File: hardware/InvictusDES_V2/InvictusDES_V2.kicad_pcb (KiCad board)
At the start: 4 copper layers, 53.7 x 40.9 mm, 73 parts, among them J1 Screw_Terminal_01x02, J10 USB_B_Micro, J11 Conn_01x06, J12 Micro_SD_Card, J2 Conn_02x05_Odd_Even, J3 Conn_01x06, J9 Conn_01x04, U1 TPSM863257RDXR, U2 STM32F405RGTx, U3 TPS2116DRL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

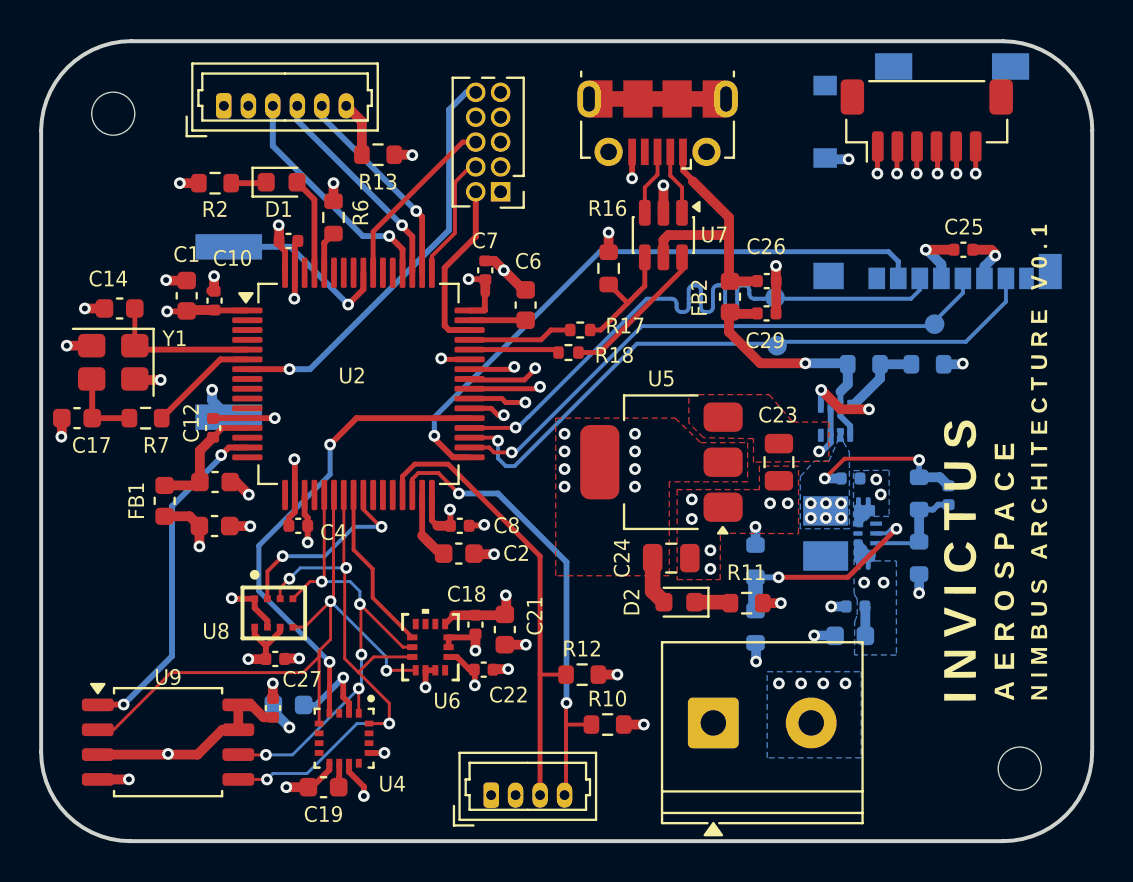
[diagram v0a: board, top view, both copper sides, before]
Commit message: Connectors made to JST-SH, aligned silkscreen designators and connectors
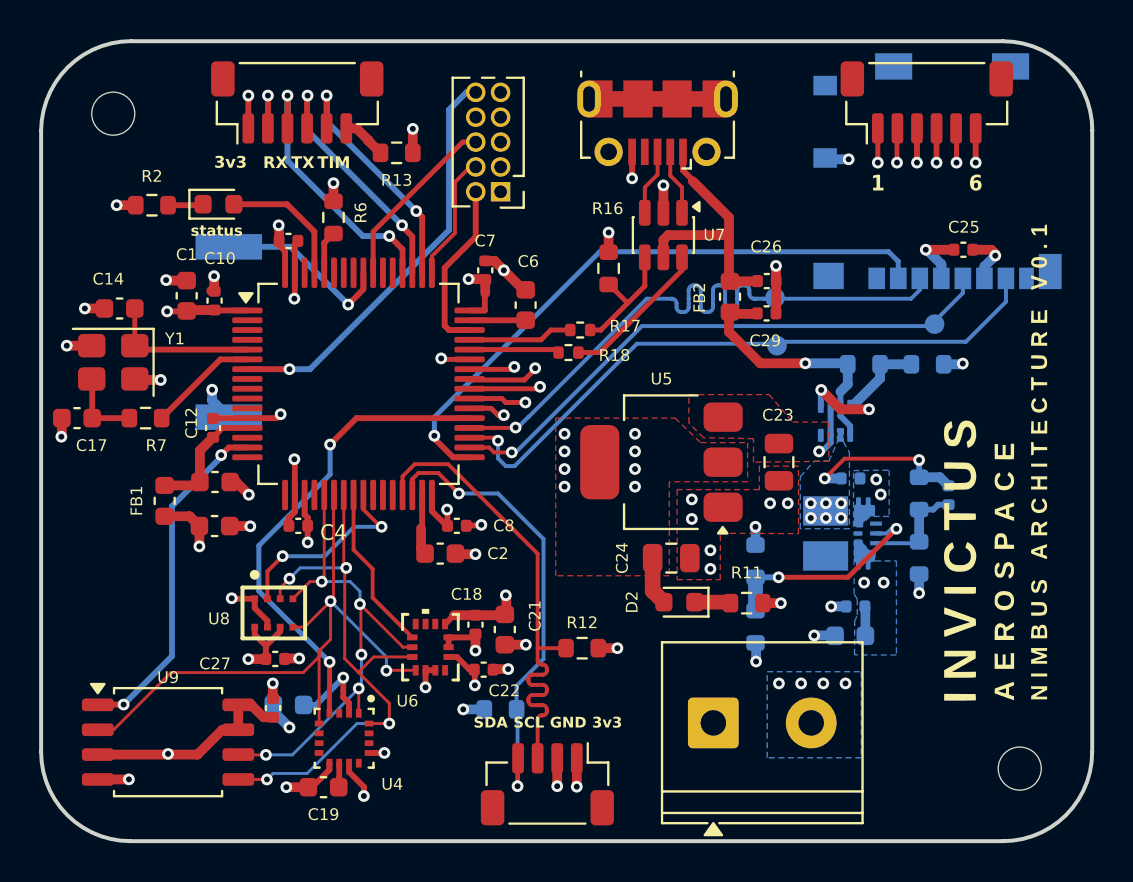
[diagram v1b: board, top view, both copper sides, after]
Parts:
- J11: footprint Connector_Molex:Molex_PicoBlade_53047-0610_1x06_P1.25mm_Vertical -> Connector_JST:JST_SH_BM06B-SRSS-TB_1x06-1MP_P1.00mm_Vertical
- J9: footprint Connector_Molex:Molex_PicoBlade_53047-0410_1x04_P1.25mm_Vertical -> Connector_JST:JST_SH_BM04B-SRSS-TB_1x04-1MP_P1.00mm_Vertical
- R10: moved to B.Cu
- moved R10 5.53 mm to (118.6, 121.1), turned to 0 degrees
- moved J11 3.75 mm to (108.2, 90.1)
- moved D1 3.42 mm to (104.2, 95.3)
- moved R2 3.42 mm to (100.8, 95.4)
- moved J9 2.93 mm to (121.0, 125.0), turned to 180 degrees
- moved R12 1.35 mm to (122.8, 118.0)
- moved R13 0.95 mm to (113.3, 92.7)
- moved C2 0.95 mm to (115.5, 113.2)
- moved J3 0.92 mm to (140.3, 90.1)
- moved C8 0.15 mm to (116.3, 111.8)
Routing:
- net GND: track 70.2 -> 73.7 mm, vias 49 -> 51
- net +3V3: track 55.7 -> 58.7 mm, vias 25 -> 27
- net USART3_TX: track 11.0 -> 13.6 mm, vias 1 -> 2
- net TIM2_CH1: track 10.6 -> 12.8 mm, vias 1 -> 2
- net USART3_RX: track 12.1 -> 13.9 mm, vias 1 -> 2
- net LED_STATUS: track 4.99 -> 6.79 mm
- net I2C2_SCL: track 23.7 -> 25.4 mm
- net SERVO_4: track 31.1 -> 32.1 mm
- net SERVO_3: track 29.9 -> 30.9 mm
- net SERVO_1: track 30.2 -> 31.1 mm
- net SERVO_2: track 28.8 -> 29.7 mm
- net SERVO_5: track 33.2 -> 34.1 mm
- net SERVO_6: track 35.2 -> 36.0 mm
- net Net-(J11-Pin_6): track 2.83 -> 2.28 mm
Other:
- board text added: "1"
- board text added: "3v3"
- board text added: "6"
- board text added: "GND"
- board text added: "RX"
- board text added: "SCL"
- board text added: "SDA"
- board text added: "TIM"
- board text added: "TX"
- board text added: "status"

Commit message: keep-out zones for IMU, Mag filled.
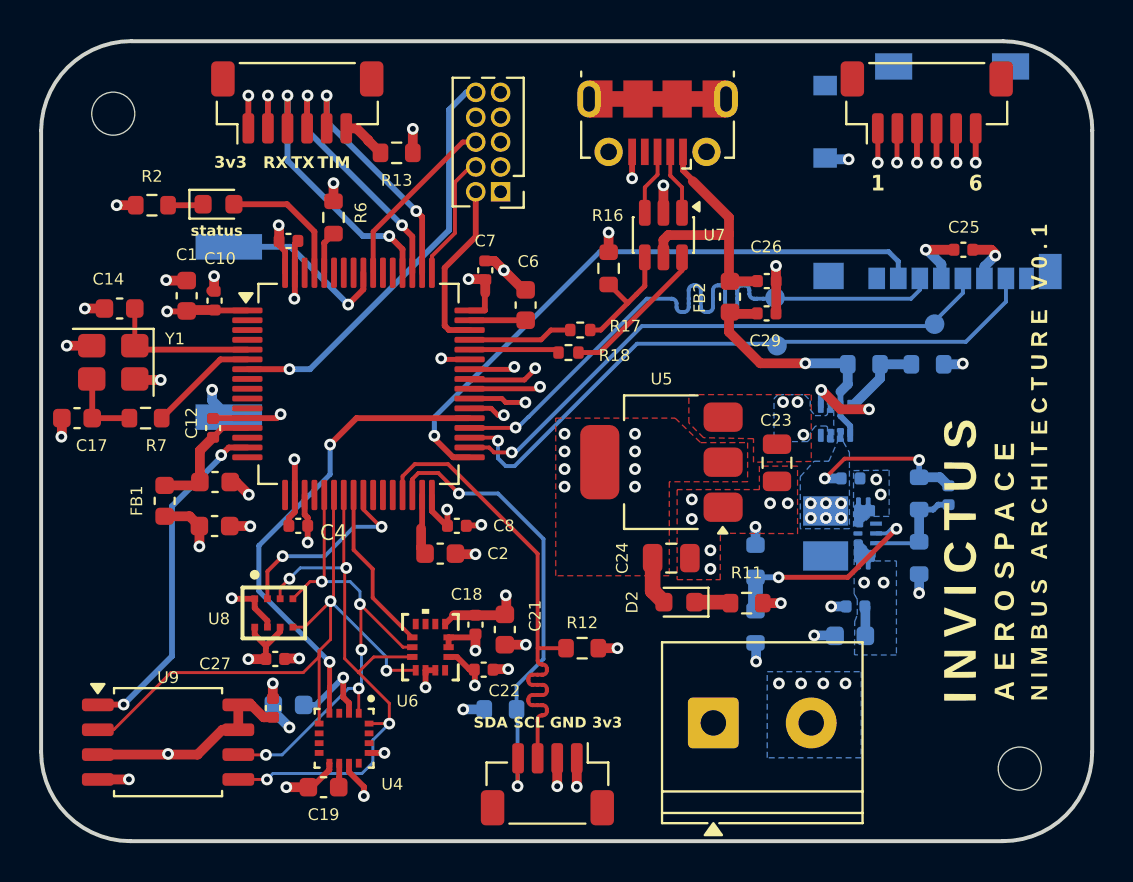
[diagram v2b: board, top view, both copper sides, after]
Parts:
- moved C23 0.10 mm to (132.7, 108.5)
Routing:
- net 5V_MUX: track 2.74 -> 0.11 mm, vias 1 -> 3
- net SPI1_MOSI: track 30.1 -> 30.7 mm
- added copper zone on B.Cu, net 5V_MUX
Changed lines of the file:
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@@
 			(outputformat 1)
 			(mirror no)
-			(drillshape 1)
+			(drillshape 0)
 			(scaleselection 1)
-			(outputdirectory "")
+			(outputdirectory "./")
 		)
 	)
@@
 		(tags "resistor")
 		(property "Reference" "R16"
-			(at 3.05 -0.05 0)
+			(at 2.7 -0.05 0)
 			(layer "F.SilkS")
 			(effects
@@
 	(footprint "Capacitor_SMD:C_0805_2012Metric"
 		(layer "F.Cu")
-		(at 132.8 108.5 -90)
+		(at 132.7 108.53 -90)
 		(descr "Capacitor SMD 0805 (2012 Metric), square (rectangular) end terminal, IPC-7351 nominal, (Body size source: IPC-SM-782 page 76, https://www.pcb-3d.com/wordpress/wp-content/uploads/ipc-sm-782a_amendment_1_and_2.pdf, https://docs.google.com/spreadsheets/d/1BsfQQcO9C6DZCsRaXUlFlo91Tg2WpOkGARC1WS5S8t0/edit?usp=sharing), generated with kicad-footprint-generator")
 		(tags "capacitor")
@@
 		)
 		(fp_text user "${REFERENCE}"
-			(at -2.4 0.05 180)
+			(at -2.17 0.05 180)
 			(layer "F.SilkS")
 			(effects
@@
 		(tags "SOT-583-8")
 		(property "Reference" "U3"
-			(at 0.161875 2.39 0)
+			(at -1.958125 1.78 0)
 			(unlocked yes)
 			(layer "B.SilkS")
@@
 	)
 	(via
-		(at 134.85 107.95)
+		(at 133.01 105.43)
 		(size 0.6)
 		(drill 0.3)
 		(layers "F.Cu" "B.Cu")
+		(free yes)
 		(net 7)
 	)
-	(segment
-		(start 135.44 107.513729)
-		(end 135.003729 107.95)
-		(width 0.3)
-		(layer "B.Cu")
-		(net 7)
-	)
-	(segment
-		(start 135.44 107.128125)
-		(end 135.44 105.648125)
-		(width 0.3)
-		(layer "B.Cu")
-		(net 7)
-	)
-	(segment
-		(start 135.003729 107.95)
-		(end 134.85 107.95)
-		(width 0.3)
-		(layer "B.Cu")
+	(via
+		(at 134.05 107.1)
+		(size 0.6)
+		(drill 0.3)
+		(layers "F.Cu" "B.Cu")
+		(free yes)
 		(net 7)
 	)
-	(segment
-		(start 135.44 107.128125)
-		(end 135.44 107.513729)
-		(width 0.3)
-		(layer "B.Cu")
+	(via
+		(at 133.75 105.43)
+		(size 0.6)
+		(drill 0.3)
+		(layers "F.Cu" "B.Cu")
+		(free yes)
 		(net 7)
 	)
@@
 	)
 	(segment
-		(start 135.94 105.648125)
-		(end 135.94 104.898125)
+		(start 135.94 106.146875)
+		(end 135.94 105.648125)
 		(width 0.3)
 		(layer "B.Cu")
@@
 	)
 	(segment
-		(start 135.94 106.146875)
-		(end 135.94 105.648125)
-		(width 0.3)
+		(start 135.94 104.898125)
+		(end 136.315 104.523125)
+		(width 0.5)
 		(layer "B.Cu")
 		(net 17)
@@
 	)
 	(segment
-		(start 135.94 104.898125)
-		(end 136.315 104.523125)
-		(width 0.5)
+		(start 135.94 105.648125)
+		(end 135.94 104.898125)
+		(width 0.3)
 		(layer "B.Cu")
 		(net 17)
@@
 	)
 	(segment
+		(start 141.9 96.95)
+		(end 141.9 93.23)
+		(width 0.254)
+		(layer "In1.Cu")
+		(net 31)
+	)
+	(segment
 		(start 141.87 93.1)
 		(end 141.87 93.2)
@@
 	)
 	(segment
-		(start 133.4 105.45)
-		(end 119.85 105.45)
+		(start 141.9 93.23)
+		(end 141.87 93.2)
 		(width 0.254)
 		(layer "In1.Cu")
@@
 	)
 	(segment
-		(start 141.9 96.95)
-		(end 133.4 105.45)
+		(start 134.29 104.56)
+		(end 141.9 96.95)
 		(width 0.254)
 		(layer "In1.Cu")
@@
 	)
 	(segment
-		(start 141.87 93.2)
-		(end 141.9 93.23)
+		(start 119.85 105.45)
+		(end 131.53 105.45)
 		(width 0.254)
 		(layer "In1.Cu")
@@
 	)
 	(segment
-		(start 141.9 93.23)
-		(end 141.9 96.95)
+		(start 132.42 104.56)
+		(end 134.29 104.56)
+		(width 0.254)
+		(layer "In1.Cu")
+		(net 31)
+	)
+	(segment
+		(start 131.53 105.45)
+		(end 132.42 104.56)
 		(width 0.254)
 		(layer "In1.Cu")
@@
 	)
 	(segment
-		(start 112.9 121.85)
-		(end 111.25 121.85)
+		(start 106.65 124.705)
+		(end 106.955 124.4)
 		(width 0.15)
 		(layer "B.Cu")
@@
 	)
 	(segment
+		(start 112.06 122.69)
+		(end 112.9 121.85)
+		(width 0.15)
+		(layer "B.Cu")
+		(net 46)
+	)
+	(segment
 		(start 106.955 124.4)
-		(end 106.65 124.705)
+		(end 111.5 124.4)
 		(width 0.15)
 		(layer "B.Cu")
@@
 	)
 	(segment
-		(start 108.7 124.4)
-		(end 106.955 124.4)
+		(start 112.06 123.84)
+		(end 112.06 122.69)
 		(width 0.15)
 		(layer "B.Cu")
@@
 	)
 	(segment
-		(start 111.25 121.85)
-		(end 108.7 124.4)
+		(start 111.5 124.4)
+		(end 112.06 123.84)
 		(width 0.15)
 		(layer "B.Cu")
@@
 	)
 	(via
-		(at 111.477354 118.327354)
+		(at 111.477354 118.077354)
 		(size 0.6)
 		(drill 0.3)
@@
 	)
 	(segment
-		(start 111.338638 120.054577)
-		(end 111.345423 120.054577)
-		(width 0.15)
-		(layer "B.Cu")
-		(net 50)
-	)
-	(segment
 		(start 111.4 115.75)
 		(end 111.4 115.1)
@@
 	)
 	(segment
-		(start 111.345423 120.054577)
-		(end 111.477354 119.922646)
+		(start 107.42 123.45)
+		(end 106.6 123.45)
 		(width 0.15)
 		(layer "B.Cu")
@@
 	)
 	(segment
-		(start 111.338638 120.061362)
-		(end 107.95 123.45)
+		(start 111.4 115.1)
+		(end 110.9 114.6)
 		(width 0.15)
 		(layer "B.Cu")
@@
 	)
 	(segment
-		(start 111.4 115.1)
-		(end 110.9 114.6)
+		(start 111.338638 120.054577)
+		(end 110.815423 120.054577)
 		(width 0.15)
 		(layer "B.Cu")
@@
 	(segment
 		(start 111.477354 119.922646)
-		(end 111.477354 118.327354)
+		(end 111.345423 120.054577)
 		(width 0.15)
 		(layer "B.Cu")
@@
 	)
 	(segment
-		(start 107.95 123.45)
-		(end 106.6 123.45)
+		(start 110.815423 120.054577)
+		(end 107.42 123.45)
 		(width 0.15)
 		(layer "B.Cu")
@@
 	)
 	(segment
-		(start 111.338638 120.054577)
-		(end 111.338638 120.061362)
+		(start 111.345423 120.054577)
+		(end 111.338638 120.054577)
+		(width 0.15)
+		(layer "B.Cu")
+		(net 50)
+	)
+	(segment
+		(start 111.477354 118.077354)
+		(end 111.477354 119.922646)
 		(width 0.15)
 		(layer "B.Cu")
@@
 		(priority 4)
 		(connect_pads yes
-			(clearance 0.4)
+			(clearance 0.3)
 		)
 		(min_thickness 0.25)
@@
 		(polygon
 			(pts
-				(xy 133.8 108.7) (xy 131.8 108.7) (xy 131.8 109.9) (xy 127.6 109.9) (xy 127.6 114.5) (xy 129.8 114.5)
-				(xy 129.81 112.13) (xy 133.8 112.15)
+				(xy 133.75 108.7) (xy 131.8 108.7) (xy 131.8 109.9) (xy 127.6 109.9) (xy 127.6 114.5) (xy 129.8 114.5)
+				(xy 129.81 112.13) (xy 133.75 112.149747)
 			)
 		)
@@
 		(polygon
 			(pts
-				(xy 135.35 108.45) (xy 131.5 108.5) (xy 131.5 107.3) (xy 128.95 107.25) (xy 128.2 106.5) (xy 128.2 105.05)
-				(xy 132.3 105.05) (xy 133.5 106.45) (xy 135.35 106.45)
+				(xy 134.45 108.461688) (xy 131.5 108.5) (xy 131.5 107.3) (xy 128.95 107.25) (xy 128.2 106.5) (xy 128.2 105.05)
+				(xy 134.45 105.05)
 			)
 		)
@@
 	)
 	(zone
+		(net 0)
+		(net_name "")
+		(layers "F.Cu" "B.Cu" "In1.Cu" "In2.Cu")
+		(name "IMU_Keepout")
+		(hatch edge 0.5)
+		(connect_pads yes
+			(clearance 0)
+		)
+		(min_thickness 0.25)
+		(filled_areas_thickness no)
+		(keepout
+			(tracks not_allowed)
+			(vias not_allowed)
+			(pads not_allowed)
+			(copperpour not_allowed)
+			(footprints allowed)
+		)
+		(placement
+			(enabled no)
+			(sheetname "")
+		)
+		(fill
+			(thermal_gap 0.5)
+			(thermal_bridge_width 0.5)
+			(smoothing fillet)
+			(radius 0.05)
+		)
+		(polygon
+			(pts
+				(xy 114.43 117.146699) (xy 115.57 117.146699) (xy 115.57 118.756699) (xy 114.43 118.756699)
+			)
+		)
+	)
+	(zone
+		(net 0)
+		(net_name "")
+		(layers "F.Cu" "B.Cu" "In1.Cu" "In2.Cu")
+		(name "Mag_Keepout")
+		(hatch edge 0.5)
+		(connect_pads yes
+			(clearance 0)
+		)
+		(min_thickness 0.25)
+		(filled_areas_thickness no)
+		(keepout
+			(tracks not_allowed)
+			(vias not_allowed)
+			(pads not_allowed)
+			(copperpour not_allowed)
+			(footprints allowed)
+		)
+		(placement
+			(enabled no)
+			(sheetname "")
+		)
+		(fill
+			(thermal_gap 0.5)
+			(thermal_bridge_width 0.5)
+		)
+		(polygon
+			(pts
+				(xy 109.6 121.630831) (xy 111.58 121.630831) (xy 111.58 123.570831) (xy 109.6 123.570831)
+			)
+		)
+	)
+	(zone
 		(net 9)
 		(net_name "+VBAT")
@@
 		(priority 3)
 		(connect_pads yes
-			(clearance 0.3)
+			(clearance 0)
 		)
 		(min_thickness 0.25)
@@
 	)
 	(zone
+		(net 7)
+		(net_name "5V_MUX")
+		(layer "B.Cu")
+		(name "5V_REG_B")
+		(hatch edge 0.5)
+		(connect_pads yes
+			(clearance 0)
+		)
+		(min_thickness 0.25)
+		(filled_areas_thickness no)
+		(fill yes
+			(thermal_gap 0.5)
+			(thermal_bridge_width 0.5)
+			(smoothing fillet)
+			(radius 0.05)
+		)
+		(polygon
+			(pts
+				(xy 135.55 105.3) (xy 135.6 105.35) (xy 135.6 107.43) (xy 135.57 107.47) (xy 135.31 107.47) (xy 135.28 107.43)
+				(xy 135.28 106.7) (xy 135.22 106.65) (xy 134.67 106.65) (xy 134.41 106.97) (xy 134.41 107.29) (xy 134.26 107.45)
+				(xy 132.75 107.45) (xy 132.55 107.25) (xy 132.55 105.25) (xy 132.75 105.05) (xy 134.1 105.05) (xy 134.4 105.35)
+				(xy 134.39 105.8) (xy 134.64 106.12) (xy 135.21 106.12) (xy 135.28 106.05) (xy 135.28 105.35) (xy 135.32 105.3)
+			)
+		)
+	)
+	(zone
 		(net 2)
 		(net_name "GND")
@@
 		)
 	)
+	(group ""
+		(members "71e9c888-852d-4ead-abe6-902f86013b02")
+	)
 	(generated

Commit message: Layout tidying. Labeled all GPIOs. 0 DRC violations.
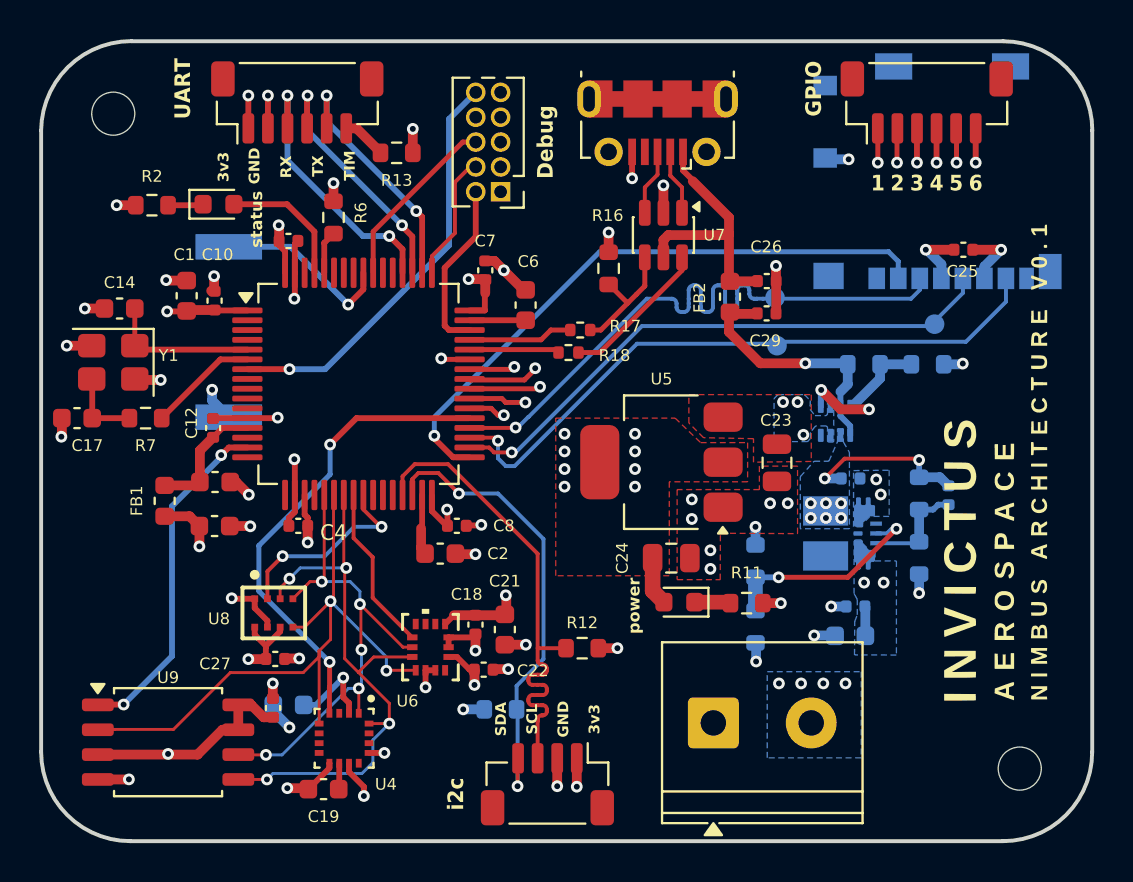
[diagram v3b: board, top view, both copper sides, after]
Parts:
- added G***: LOGO, LOGO, B.Cu at (102.1, 114.8)
- moved C19 0.10 mm to (109.5, 125.2)
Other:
- board text added: "2"
- board text added: "3"
- board text added: "4"
- board text added: "5"
- board text added: "Debug"
- board text added: "GPIO"
- board text added: "UART"
- board text added: "i2c"
- board text added: "power"
